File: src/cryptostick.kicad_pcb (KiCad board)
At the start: 2 copper layers, 21.8 x 16.3 mm, 33 parts, among them J1 SIM_JACKET, J2 USB_A, P1 CONN_4, U1 STM32F103TB, U2 CAT6217-330, U3 DF5A5.6JE, X1 12MHz, p1 debug-pin, p2 debug-pin, p3 debug-pin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

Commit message: ticks added
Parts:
- added REF**: Fiducial_0.5mm_Dia_1mm_Outer, Fiducial:Fiducial_0.5mm_Dia_1mm_Outer, B.Cu at (135.6, 106.3)
- added REF**: Fiducial_0.5mm_Dia_1mm_Outer, Fiducial:Fiducial_0.5mm_Dia_1mm_Outer, F.Cu at (115.6, 91.8)
- added REF**: Fiducial_0.5mm_Dia_1mm_Outer, Fiducial:Fiducial_0.5mm_Dia_1mm_Outer, F.Cu at (135.6, 106.3)
- added REF**: Fiducial_0.5mm_Dia_1mm_Outer, Fiducial:Fiducial_0.5mm_Dia_1mm_Outer, B.Cu at (115.6, 91.8)
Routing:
- net /BOOT0: track 8.84 -> 6.14 mm
- net +3.3V: track 51.7 -> 54.2 mm
- net /BOOT1: track 8.12 -> 6.61 mm
- net N-0000020: track 12.7 -> 11.2 mm
- net /SCRST: track 17.1 -> 18.4 mm
- net N-0000034: track 14.1 -> 12.8 mm
- net /SCVCC: track 21.7 -> 20.6 mm
- net /SCSDA: track 18.1 -> 19.1 mm
- net /SWDIO: track 22.0 -> 21.0 mm
- net /OSC_OUT: track 18.0 -> 17.0 mm
- net /SWCLK: track 19.5 -> 18.9 mm
- net GND: track 160.2 -> 160.0 mm, vias 12 -> 13
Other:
- board text added: "R3"
- board text removed: "V2"
- board text removed: "efsffe"

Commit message: Corrections of fabrication data
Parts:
- REF** (x3): footprint Fiducial:Fiducial_0.5mm_Dia_1mm_Outer -> footprints:Fiducial_0.5mm_Dia_1mm_Outer
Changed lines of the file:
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@@
   (layers
     (0 Front signal)
-    (31 Back signal hide)
+    (31 Back signal)
     (32 B.Adhes user hide)
     (33 F.Adhes user hide)
-    (34 B.Paste user hide)
-    (35 F.Paste user hide)
-    (36 B.SilkS user hide)
-    (37 F.SilkS user hide)
-    (38 B.Mask user hide)
+    (34 B.Paste user)
+    (35 F.Paste user)
+    (36 B.SilkS user)
+    (37 F.SilkS user)
+    (38 B.Mask user)
     (39 F.Mask user)
     (40 Dwgs.User user hide)
@@
     (add_net +3.3V)
   )
+  (module footprints:Fiducial_0.5mm_Dia_1mm_Outer (layer Front)
+    (at 135.56 106.35)
+    (descr "Circular Fiducial, 0.5mm bare copper top; 1mm keepout (Level C)")
+    (tags marker)
+    (attr virtual)
+    (fp_text reference REF** (at 0 -1.5) (layer F.SilkS) hide
+      (effects (font (size 1 1) (thickness 0.15)))
+    )
+    (fp_text value Fiducial_0.5mm_Dia_1mm_Outer (at 0 1.5) (layer F.Fab)
+      (effects (font (size 1 1) (thickness 0.15)))
+    )
+    (fp_circle (center 0 0) (end 0.1 0) (layer F.Paste) (width 0.3))
+    (fp_circle (center 0 0) (end 0.5 0) (layer F.Fab) (width 0.1))
+    (fp_text user %R (at 0 0) (layer F.Fab)
+      (effects (font (size 0.2 0.2) (thickness 0.04)))
+    )
+    (fp_circle (center 0 0) (end 0.75 0) (layer F.CrtYd) (width 0.05))
+    (pad ~ smd circle (at 0 0) (size 0.5 0.5) (layers Front F.Mask)
+      (solder_mask_margin 0.25) (clearance 0.25))
+  )
+  (module footprints:Fiducial_0.5mm_Dia_1mm_Outer (layer Back)
+    (at 115.56 91.85)
+    (descr "Circular Fiducial, 0.5mm bare copper top; 1mm keepout (Level C)")
+    (tags marker)
+    (attr virtual)
+    (fp_text reference REF** (at 0 1.5) (layer B.SilkS) hide
+      (effects (font (size 1 1) (thickness 0.15)) (justify mirror))
+    )
+    (fp_text value Fiducial_0.5mm_Dia_1mm_Outer (at 0 -1.5) (layer B.Fab) hide
+      (effects (font (size 1 1) (thickness 0.15)) (justify mirror))
+    )
+    (fp_circle (center 0 0) (end 0.1 0) (layer B.Paste) (width 0.3))
+    (fp_circle (center 0 0) (end 0.5 0) (layer B.Fab) (width 0.1))
+    (fp_text user %R (at 0 0) (layer B.Fab)
+      (effects (font (size 0.2 0.2) (thickness 0.04)) (justify mirror))
+    )
+    (fp_circle (center 0 0) (end 0.75 0) (layer B.CrtYd) (width 0.05))
+    (pad ~ smd circle (at 0 0) (size 0.5 0.5) (layers Back B.Mask)
+      (solder_mask_margin 0.25) (clearance 0.25))
+  )
+  (module footprints:Fiducial_0.5mm_Dia_1mm_Outer (layer Front)
+    (at 115.56 91.85)
+    (descr "Circular Fiducial, 0.5mm bare copper top; 1mm keepout (Level C)")
+    (tags marker)
+    (attr virtual)
+    (fp_text reference REF** (at 0 -1.5) (layer F.SilkS) hide
+      (effects (font (size 1 1) (thickness 0.15)))
+    )
+    (fp_text value Fiducial_0.5mm_Dia_1mm_Outer (at 0 1.5) (layer F.Fab)
+      (effects (font (size 1 1) (thickness 0.15)))
+    )
+    (fp_circle (center 0 0) (end 0.1 0) (layer F.Paste) (width 0.3))
+    (fp_circle (center 0 0) (end 0.5 0) (layer F.Fab) (width 0.1))
+    (fp_text user %R (at 0 0) (layer F.Fab)
+      (effects (font (size 0.2 0.2) (thickness 0.04)))
+    )
+    (fp_circle (center 0 0) (end 0.75 0) (layer F.CrtYd) (width 0.05))
+    (pad ~ smd circle (at 0 0) (size 0.5 0.5) (layers Front F.Mask)
+      (solder_mask_margin 0.25) (clearance 0.25))
+  )
   (module Fiducial:Fiducial_0.5mm_Dia_1mm_Outer (layer Back)
     (at 135.56 106.35)
@@
     )
     (fp_circle (center 0 0) (end 0.75 0) (layer B.CrtYd) (width 0.05))
+    (fp_circle (center 0 0) (end 0.1 0) (layer B.Paste) (width 0.3))
     (pad ~ smd circle (at 0 0) (size 0.5 0.5) (layers Back B.Mask)
       (solder_mask_margin 0.25) (clearance 0.25))
@@
     )
   )
-  (module Fiducial:Fiducial_0.5mm_Dia_1mm_Outer (layer Front)
-    (at 115.56 91.85)
-    (descr "Circular Fiducial, 0.5mm bare copper top; 1mm keepout (Level C)")
-    (tags marker)
-    (attr virtual)
-    (fp_text reference REF** (at 0 -1.5) (layer F.SilkS) hide
-      (effects (font (size 1 1) (thickness 0.15)))
-    )
-    (fp_text value Fiducial_0.5mm_Dia_1mm_Outer (at 0 1.5) (layer F.Fab)
-      (effects (font (size 1 1) (thickness 0.15)))
-    )
-    (fp_circle (center 0 0) (end 0.75 0) (layer F.CrtYd) (width 0.05))
-    (fp_text user %R (at 0 0) (layer F.Fab)
-      (effects (font (size 0.2 0.2) (thickness 0.04)))
-    )
-    (fp_circle (center 0 0) (end 0.5 0) (layer F.Fab) (width 0.1))
-    (pad ~ smd circle (at 0 0) (size 0.5 0.5) (layers Front F.Mask)
-      (solder_mask_margin 0.25) (clearance 0.25))
-  )
-  (module Fiducial:Fiducial_0.5mm_Dia_1mm_Outer (layer Front)
-    (at 135.56 106.35)
-    (descr "Circular Fiducial, 0.5mm bare copper top; 1mm keepout (Level C)")
-    (tags marker)
-    (attr virtual)
-    (fp_text reference REF** (at 0 -1.5) (layer F.SilkS) hide
-      (effects (font (size 1 1) (thickness 0.15)))
-    )
-    (fp_text value Fiducial_0.5mm_Dia_1mm_Outer (at 0 1.5) (layer F.Fab)
-      (effects (font (size 1 1) (thickness 0.15)))
-    )
-    (fp_circle (center 0 0) (end 0.75 0) (layer F.CrtYd) (width 0.05))
-    (fp_text user %R (at 0 0) (layer F.Fab)
-      (effects (font (size 0.2 0.2) (thickness 0.04)))
-    )
-    (fp_circle (center 0 0) (end 0.5 0) (layer F.Fab) (width 0.1))
-    (pad ~ smd circle (at 0 0) (size 0.5 0.5) (layers Front F.Mask)
-      (solder_mask_margin 0.25) (clearance 0.25))
-  )
-  (module Fiducial:Fiducial_0.5mm_Dia_1mm_Outer (layer Back)
-    (at 115.56 91.85)
-    (descr "Circular Fiducial, 0.5mm bare copper top; 1mm keepout (Level C)")
-    (tags marker)
-    (attr virtual)
-    (fp_text reference REF** (at 0 1.5) (layer B.SilkS) hide
-      (effects (font (size 1 1) (thickness 0.15)) (justify mirror))
-    )
-    (fp_text value Fiducial_0.5mm_Dia_1mm_Outer (at 0 -1.5) (layer B.Fab) hide
-      (effects (font (size 1 1) (thickness 0.15)) (justify mirror))
-    )
-    (fp_circle (center 0 0) (end 0.75 0) (layer B.CrtYd) (width 0.05))
-    (fp_text user %R (at 0 0) (layer B.Fab)
-      (effects (font (size 0.2 0.2) (thickness 0.04)) (justify mirror))
-    )
-    (fp_circle (center 0 0) (end 0.5 0) (layer B.Fab) (width 0.1))
-    (pad ~ smd circle (at 0 0) (size 0.5 0.5) (layers Back B.Mask)
-      (solder_mask_margin 0.25) (clearance 0.25))
-  )
   (gr_text R3 (at 116.58 95.36 90) (layer B.SilkS)

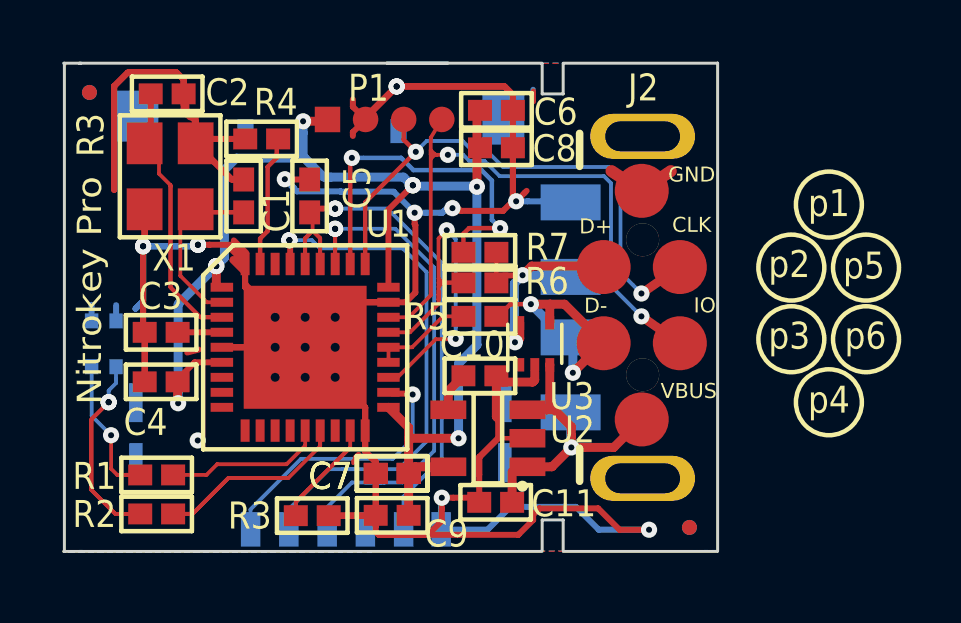
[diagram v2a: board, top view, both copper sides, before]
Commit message: Nk Pro v6 - update to KiCad v9 - add smartcard pullup (R8) - update panelization - update outputs
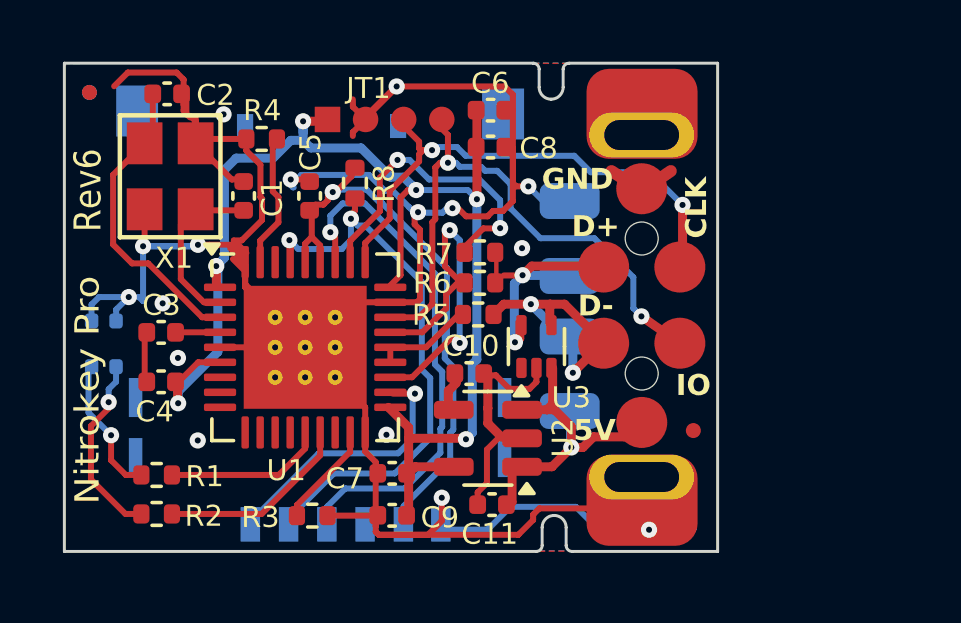
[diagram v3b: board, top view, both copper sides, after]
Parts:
- removed the C7 at (125.7, 104.5)
- added R8: 20k, Resistor_SMD:R_0402_1005Metric, F.Cu at (124.4, 94.9)
- C1, C10, C11, C2, C3, C4, C5, C6, C7, C8, C9: footprint c_0402 -> Capacitor_SMD:C_0402_1005Metric
- J2: moved to B.Cu
- R1, R2, R3, R4, R5, R6, R7: footprint r_0402 -> Resistor_SMD:R_0402_1005Metric
- U1: footprint QFN36 -> Package_DFN_QFN:QFN-36-1EP_6x6mm_P0.5mm_EP4.1x4.1mm_ThermalVias
- U2: footprint TSOT23-5 -> Package_TO_SOT_SMD:TSOT-23-5
- U3: footprint TO_SOT_Packages_SMD:SOT-553 -> Package_TO_SOT_SMD:SOT-553
- moved FID1 3.23 mm to (135.7, 103.1)
- moved J2 0.86 mm to (142.2, 98.6)
- moved C10 0.36 mm to (128.2, 101.2), turned to 0 degrees
- moved C8 0.20 mm to (128.9, 93.7), turned to 180 degrees
- moved C6 0.20 mm to (128.9, 92.4), turned to 180 degrees
- moved J1 0.17 mm to (123.2, 98.9)
- moved C11 0.14 mm to (129.0, 105.6), turned to 180 degrees
- moved U3 0.11 mm to (130.5, 100.3)
- moved p4 0.10 mm to (134.0, 102.8)
- moved R5 0.08 mm to (128.5, 99.2), turned to 0 degrees
- moved p1 0.07 mm to (134.0, 95.1)
- turned C1 to 90 degrees
- turned C2 to 0 degrees
- turned C3 to 180 degrees
- turned C4 to 0 degrees
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- renumbered REF** to FID1, REF** to FID2, REF** to FID3, REF** to FID4, P1 to JT1
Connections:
- J1 pad 6: (no net) -> unconnected-(J1-NC-Pad6)
- U1 pad 10: (no net) -> unconnected-(U1-PA3-Pad10)
- U1 pad 11: (no net) -> unconnected-(U1-PA4-Pad11)
- U1 pad 12: (no net) -> unconnected-(U1-PA5-Pad12)
- U1 pad 13: (no net) -> unconnected-(U1-PA6-Pad13)
- U1 pad 16: (no net) -> unconnected-(U1-PB1-Pad16)
- U1 pad 34: (no net) -> unconnected-(U1-PB7-Pad34)
- U1 pad 7: (no net) -> unconnected-(U1-PA0-Pad7)
- U1 pad 8: (no net) -> unconnected-(U1-PA1-Pad8)
- U1 pad 9: (no net) -> unconnected-(U1-PA2-Pad9)
- U3 pad 1: (no net) -> unconnected-(U3-C1-Pad1)
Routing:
- net GND: track 160.0 -> 108.5 mm, vias 13 -> 16
- net /OSC_OUT: track 17.0 -> 9.75 mm
- net Net-(D1-K2): track 12.8 -> 6.26 mm, vias 2 -> 1
- net +3.3V: track 54.2 -> 48.0 mm, vias 8 -> 6
- net /USB_EN: track 15.4 -> 10.4 mm
- net Net-(U1-PB0): track 11.2 -> 6.52 mm
- net /BOOT1: track 6.61 -> 3.51 mm
- net /OSC_IN: track 8.07 -> 5.03 mm
- net Net-(D1-A1): track 6.56 -> 4.54 mm
- net /BOOT0: track 6.14 -> 4.30 mm
- net /SWDIO: track 21.0 -> 19.3 mm
- net /SWCLK: track 18.9 -> 17.4 mm
- net /SCVCC: track 20.6 -> 19.0 mm, vias 2 -> 1
- net /VBUS: track 11.8 -> 10.6 mm
- net /SCRST: track 18.4 -> 17.5 mm, vias 2 -> 1
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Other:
- outline, holes or cut-outs redrawn
- net class Default removed
- net class GND removed
- net class VBUS removed
- net class VDD removed
- rule pad_to_mask_clearance: 0.05 -> 0
- board text added: "5V"
- board text added: "Rev6"
- board text removed: "R3"
- board text removed: "VBUS"
